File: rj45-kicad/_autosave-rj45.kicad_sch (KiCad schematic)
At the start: 46 parts

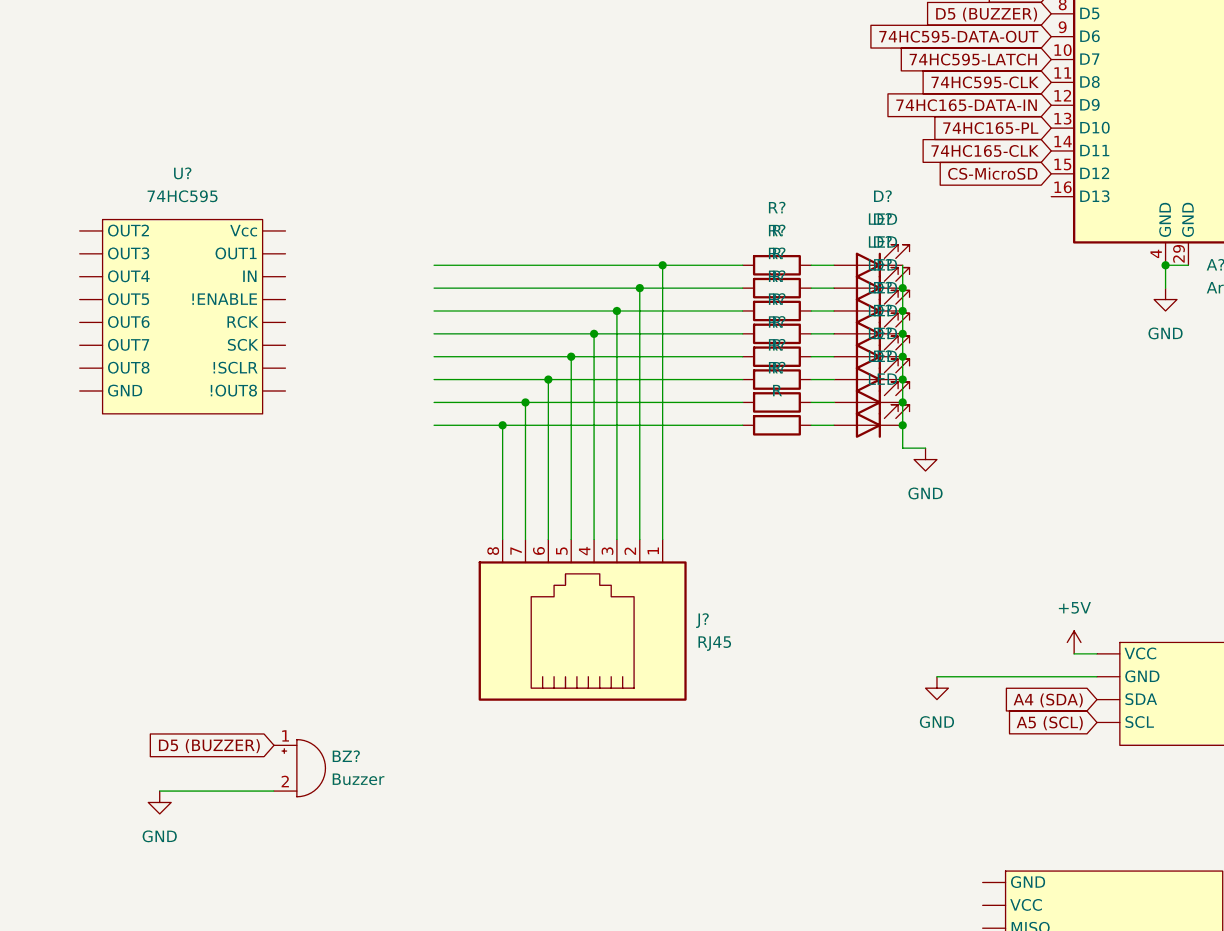
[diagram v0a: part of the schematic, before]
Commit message: Schematics using official 74HC595 shift register
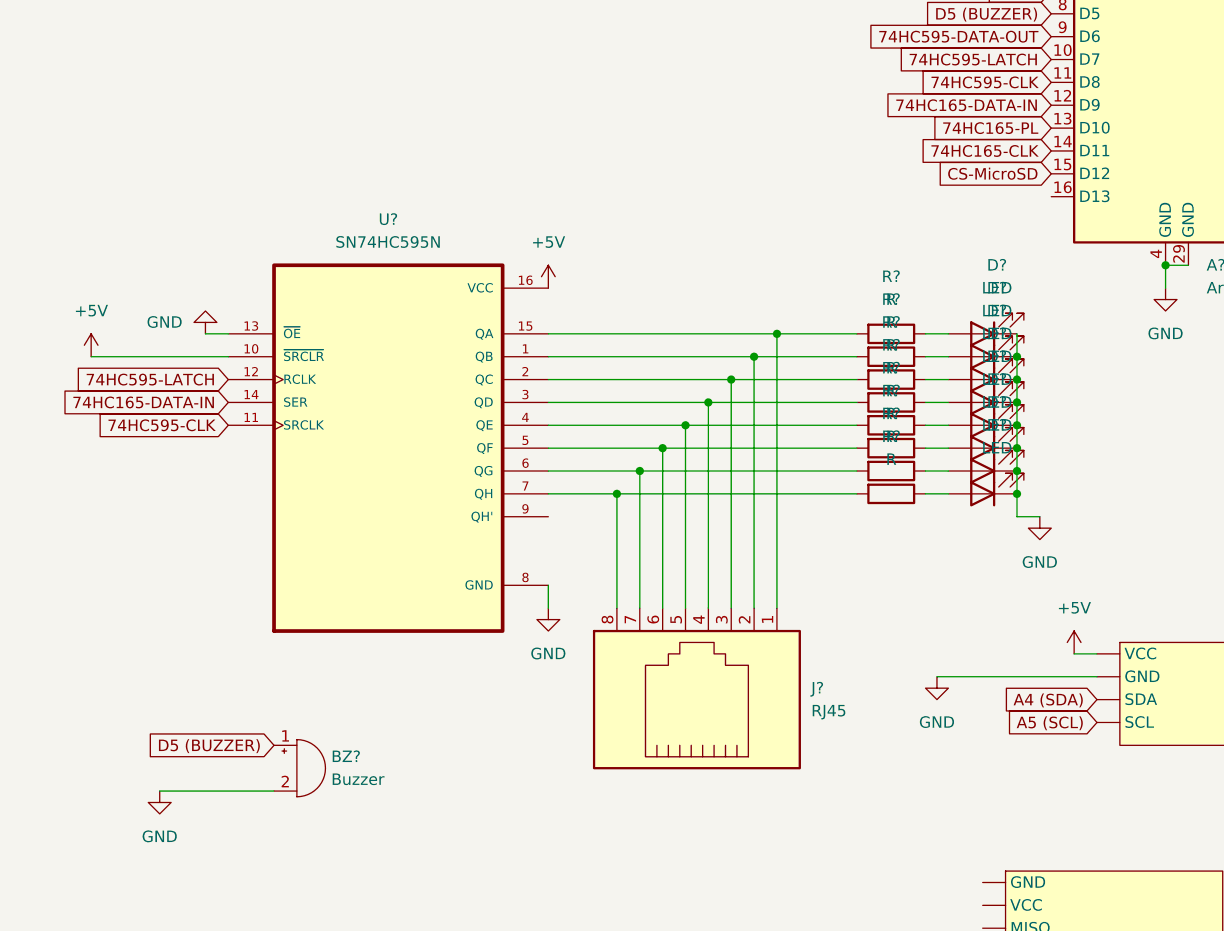
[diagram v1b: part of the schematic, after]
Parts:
- removed U?: 74HC595, symbol custom-parts:74HC595
- added U?: SN74HC595N, SN74HC595N:DIP794W45P254L1969H508Q16, symbol SN74HC595N:SN74HC595N
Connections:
- net +5V: now also U?.10 (~{SRCLR}), U?.16 (VCC)
- net 74HC165-DATA-IN: now also U?.14 (SER)
- net 74HC595-CLK: now also U?.11 (SRCLK)
- net 74HC595-LATCH: now also U?.12 (RCLK)
- net GND: now also U?.13 (~{OE}), U?.8 (GND)
- net at J?.8, R?.2: now also U?.7 (QH)
- net at J?.4, R?.2: now also U?.3 (QD)
- net at J?.1, R?.2: now also U?.15 (QA)
- net at J?.2, R?.2: now also U?.1 (QB)
- net at J?.3, R?.2: now also U?.2 (QC)
- net at J?.5, R?.2: now also U?.4 (QE)
- net at J?.6, R?.2: now also U?.5 (QF)
- net at J?.7, R?.2: now also U?.6 (QG)
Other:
- moved on the sheet: D?, J?, R?
